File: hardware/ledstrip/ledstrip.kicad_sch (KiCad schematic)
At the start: 17 parts, among them J1 Conn_ARM_JTAG_SWD_10, J2 USB_C_Receptacle_USB2.0_16P, J5 Ledstrip connector, Q1 Q_NMOS, Q2 Q_NMOS, Q3 Q_NMOS, U1 STM32G030K6Tx, U2 CP2102N-A02-GQFN20, U4 USBLC6-2SC6

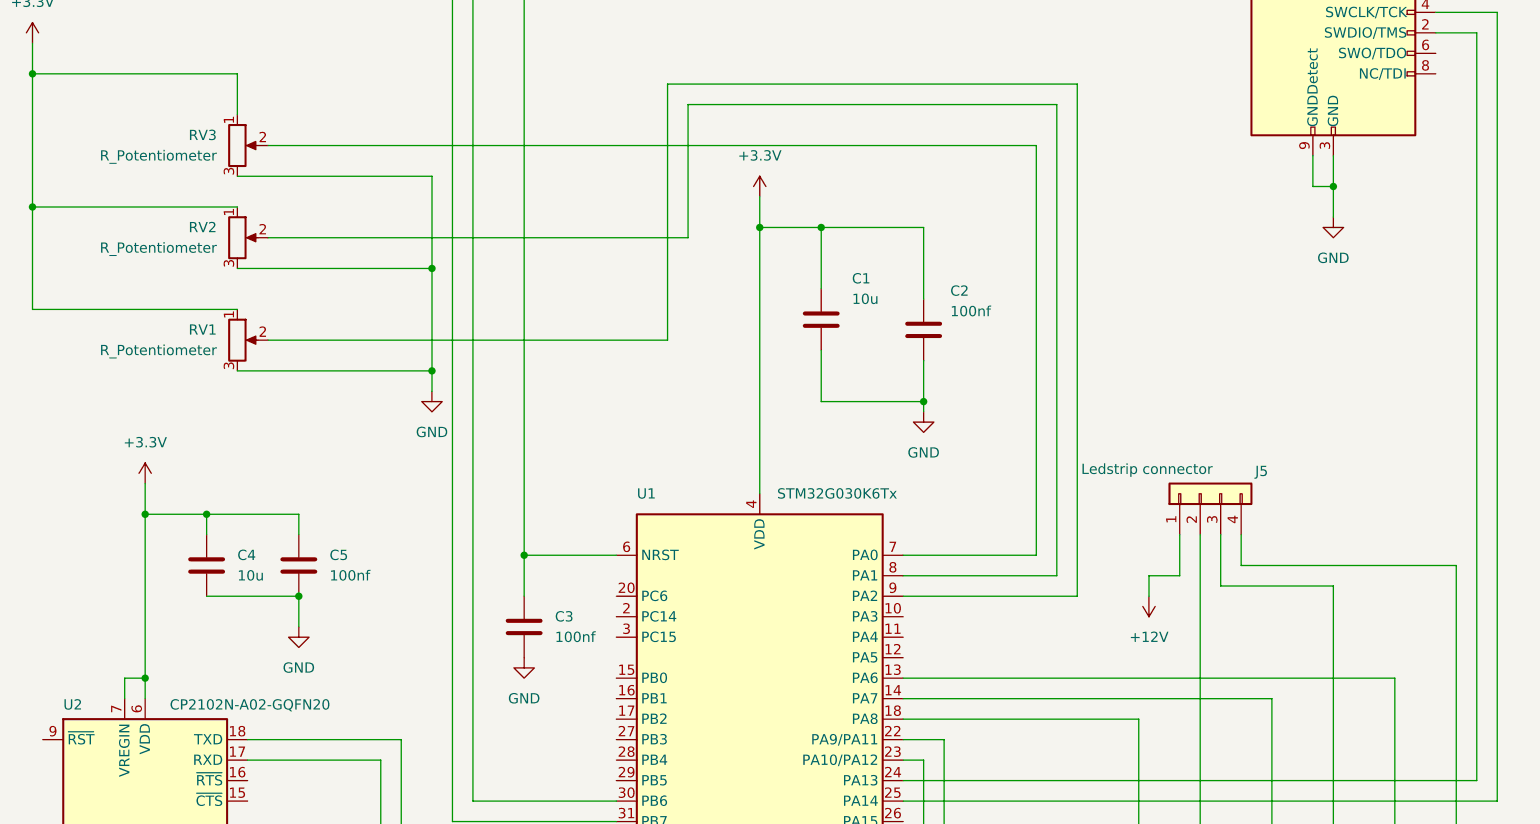
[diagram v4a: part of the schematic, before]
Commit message: Add TVS diode on VBUS line, improve STUSB4500 integration
Add P-MOSFET controled by STUSB4500 on VBUS line
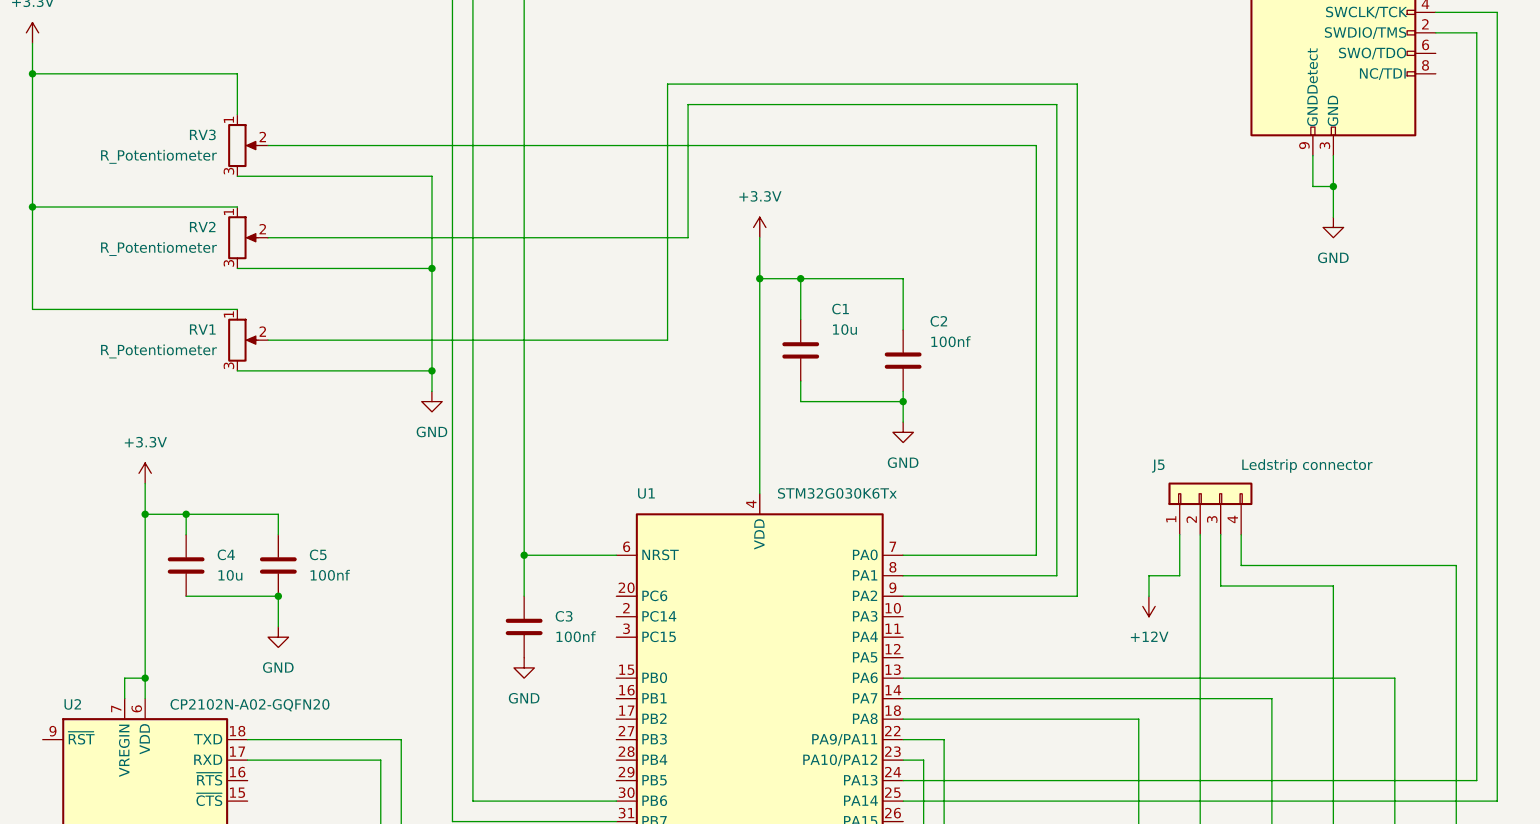
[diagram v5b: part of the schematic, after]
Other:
- moved on the sheet: C1, C2, C4, C5

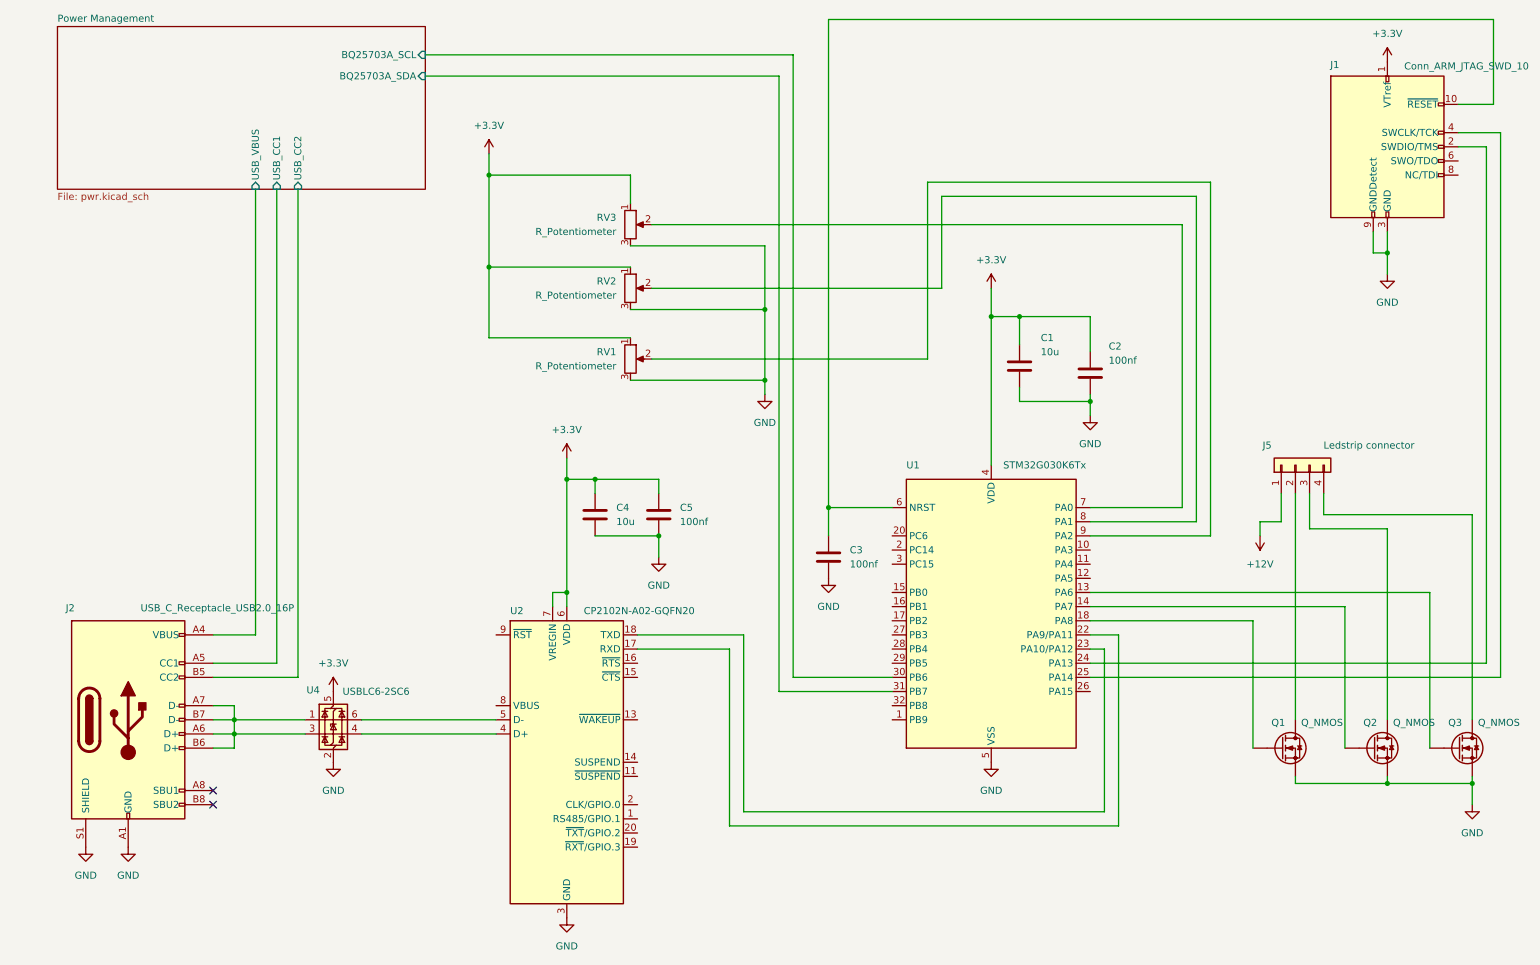
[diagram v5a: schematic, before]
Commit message: Splitted into multiple sheets.
BQ25703A integrated
buck converter OK
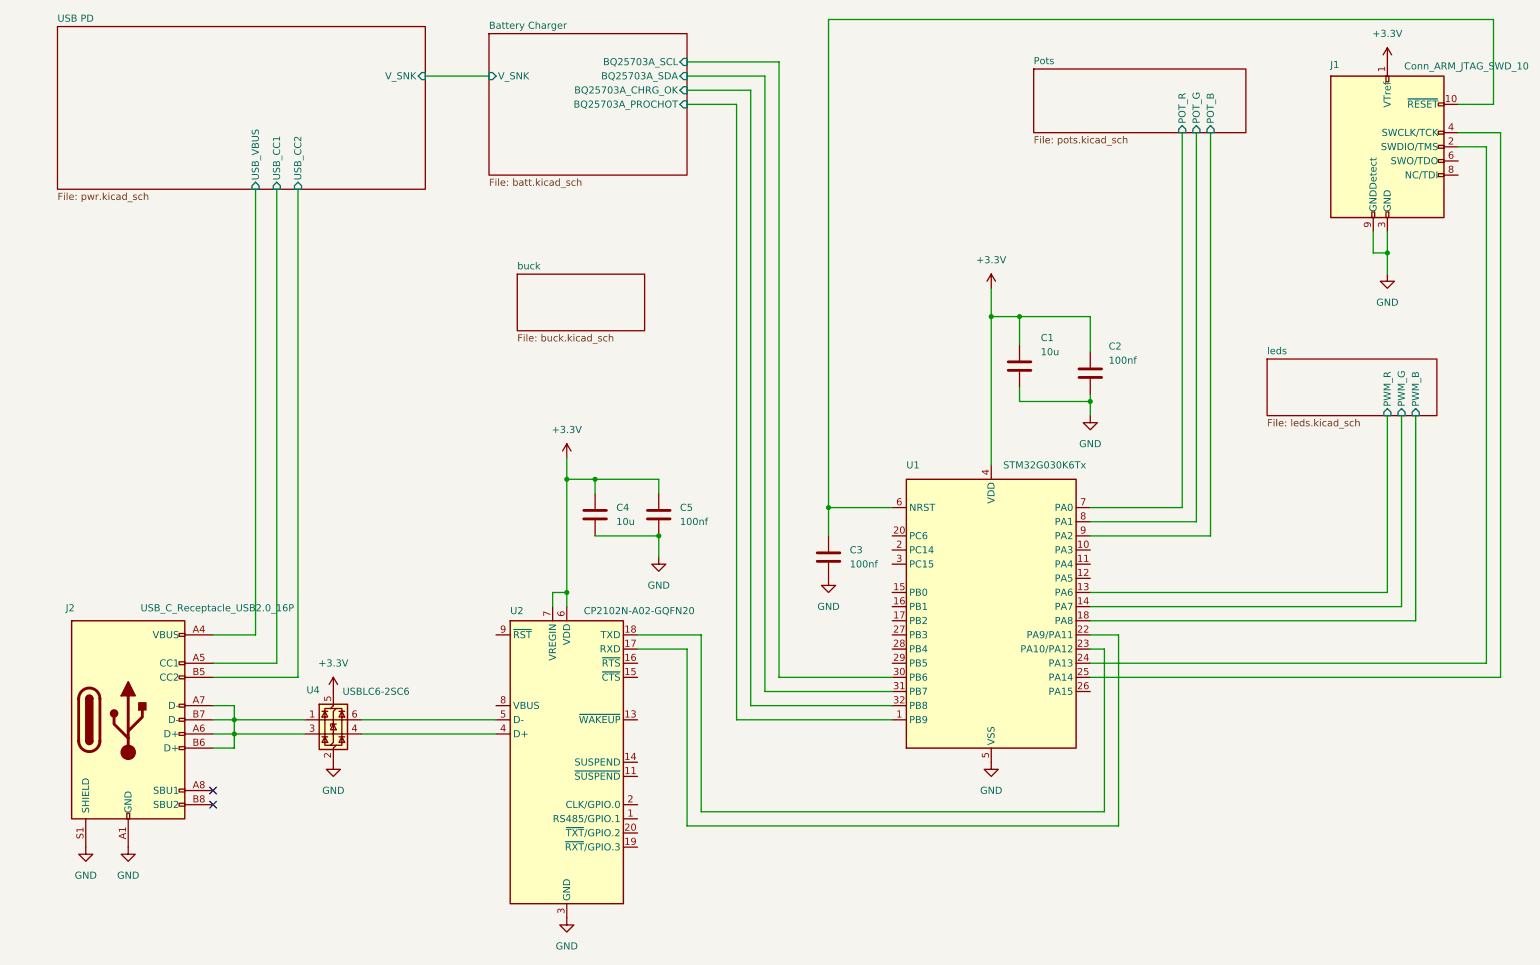
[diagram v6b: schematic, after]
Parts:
- removed J5: Ledstrip connector, Connector_JST:JST_XH_B4B-XH-A_1x04_P2.50mm_Vertical, symbol Connector_Generic:Conn_01x04
- removed Q1, Q2, Q3: Q_NMOS, Package_TO_SOT_SMD:SOT-23_Handsoldering, symbol Device:Q_NMOS
- removed RV1, RV2, RV3: R_Potentiometer, Potentiometer_THT:Potentiometer_Bourns_PTV09A-1_Single_Vertical, symbol Device:R_Potentiometer
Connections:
- net leds/PWM_G: now reaches U1.14 (PA7)
- net leds/PWM_B: now reaches U1.18 (PA8)
- net Pots/POT_G: now reaches U1.8 (PA1)
- net Pots/POT_R: now reaches U1.7 (PA0)
- net leds/PWM_R: now reaches U1.13 (PA6)
- net Pots/POT_B: now reaches U1.9 (PA2)
- net Battery Charger/BQ25703A_PROCHOT: now reaches U1.1 (PB9)
- net Battery Charger/BQ25703A_CHRG_OK: now reaches U1.32 (PB8)
- net USB PD/BQ25703A_SCL renamed Battery Charger/BQ25703A_SCL
- net USB PD/BQ25703A_SDA renamed Battery Charger/BQ25703A_SDA
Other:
- sheet Power Management renamed USB PD
- added sheet Battery Charger (batt.kicad_sch)
- added sheet Pots (pots.kicad_sch)
- added sheet buck (buck.kicad_sch)
- added sheet leds (leds.kicad_sch)
- sheet USB PD ports: added V_SNK; removed BQ25703A_SCL, BQ25703A_SDA

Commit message: Fix ERC errors.
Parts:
- added R32, R33, R34: 10k, Resistor_SMD:R_0805_2012Metric, symbol Device:R
- added TP6: TestPoint, symbol Connector:TestPoint
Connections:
- net +3.3V: now also R32.2, R33.2, R34.2
- net at U2.8 (VBUS): now also R33.1
- net at U2.9 (~{RST}): now also R32.1, TP6.1
- net at C3.1, J1.10 (~{RESET}), U1.6 (NRST): now also R34.1
- no-connect marks 2 -> 26
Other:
- moved on the sheet: U4

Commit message: Fix last errors in schematics
Missing footprint, missing distributor link.
Updated project sym-lib-table for ERC checks.
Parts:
- TP6: footprint (none) -> TestPoint:TestPoint_Pad_1.0x1.0mm
- U4: Distributor Link 1 (none) -> https://www.mouser.com/ProductDetail/STMicroelectronics/USB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; Distributor Link 2 (none) -> https://www.digikey.fr/fr/products/detail/stmicroelectronic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
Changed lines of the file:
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@@
 			)
 		)
-		(property "Footprint" ""
+		(property "Footprint" "TestPoint:TestPoint_Pad_1.0x1.0mm"
 			(at 85.09 110.49 0)
 			(effects
@@
 			(at 66.04 143.51 0)
 			(effects
+				(font
+					(size 1.27 1.27)
+				)
+				(hide yes)
+			)
+		)
+		(property "Distributor Link 1" "https://www.mouser.com/ProductDetail/STMicroelectronics/USBLC6-2SC6?qs=po45yt2pPpu%2FhNIlwQdTlg%3D%3D&srsltid=AfmBOopJbfArgk0Zhrp5NeFSS0u51o4Z8wX-JVudia6J3kfvFFcGIQE5"
+			(at 66.04 143.51 0)
+			(effects
+				(font
+					(size 1.27 1.27)
+				)
+				(hide yes)
+			)
+		)
+		(property "Distributor Link 2" "https://www.digikey.fr/fr/products/detail/stmicroelectronics/USBLC6-2SC6/1040559?srsltid=AfmBOoq_zn_3jENcYaZO0f2Fjj9ZC3iVuUou8dFQGpjlYlBu9snaol37"
+			(at 66.04 143.51 0)
+			(effects
